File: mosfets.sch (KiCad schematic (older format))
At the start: 72 parts, among them P5 CONN_01X08, P6 CONN_01X06, Q1 2N7002P, Q10 2N7002P, Q11 2N7002P, Q12 BC846BPDW1, Q13 BC846BPDW1, Q14 SI2318CDS-T1-GE3, Q15 IRFB7545PbF, Q16 2N7002P, Q17 2N7002P, Q18 BC846BPDW1, Q19 BC846BPDW1, Q2 2N7002P, Q20 SI2318CDS-T1-GE3, Q21 IRFB7545PbF, Q3 2N7002P, Q4 BC846BPDW1, Q5 BC846BPDW1, Q6 BC846BPDW1, Q7 IRFB7545PbF, Q8 SI2318CDS-T1-GE3, Q9 IRFB7545PbF

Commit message: more schematics
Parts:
- R11, R12, R21, R29: value 1K8 -> 4K7; footprint Resistors_SMD:R_0603 -> Resistors_SMD:R_0805
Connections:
- net +12V: no longer R10.1, R11.1, R12.1, R21.1, R29.1
- net Vheatbed: now also R10.1
- net Vsupply: now also R11.1, R12.1, R21.1, R29.1
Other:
- moved on the sheet: R10, R11, R12, R20, R21, R28, R29

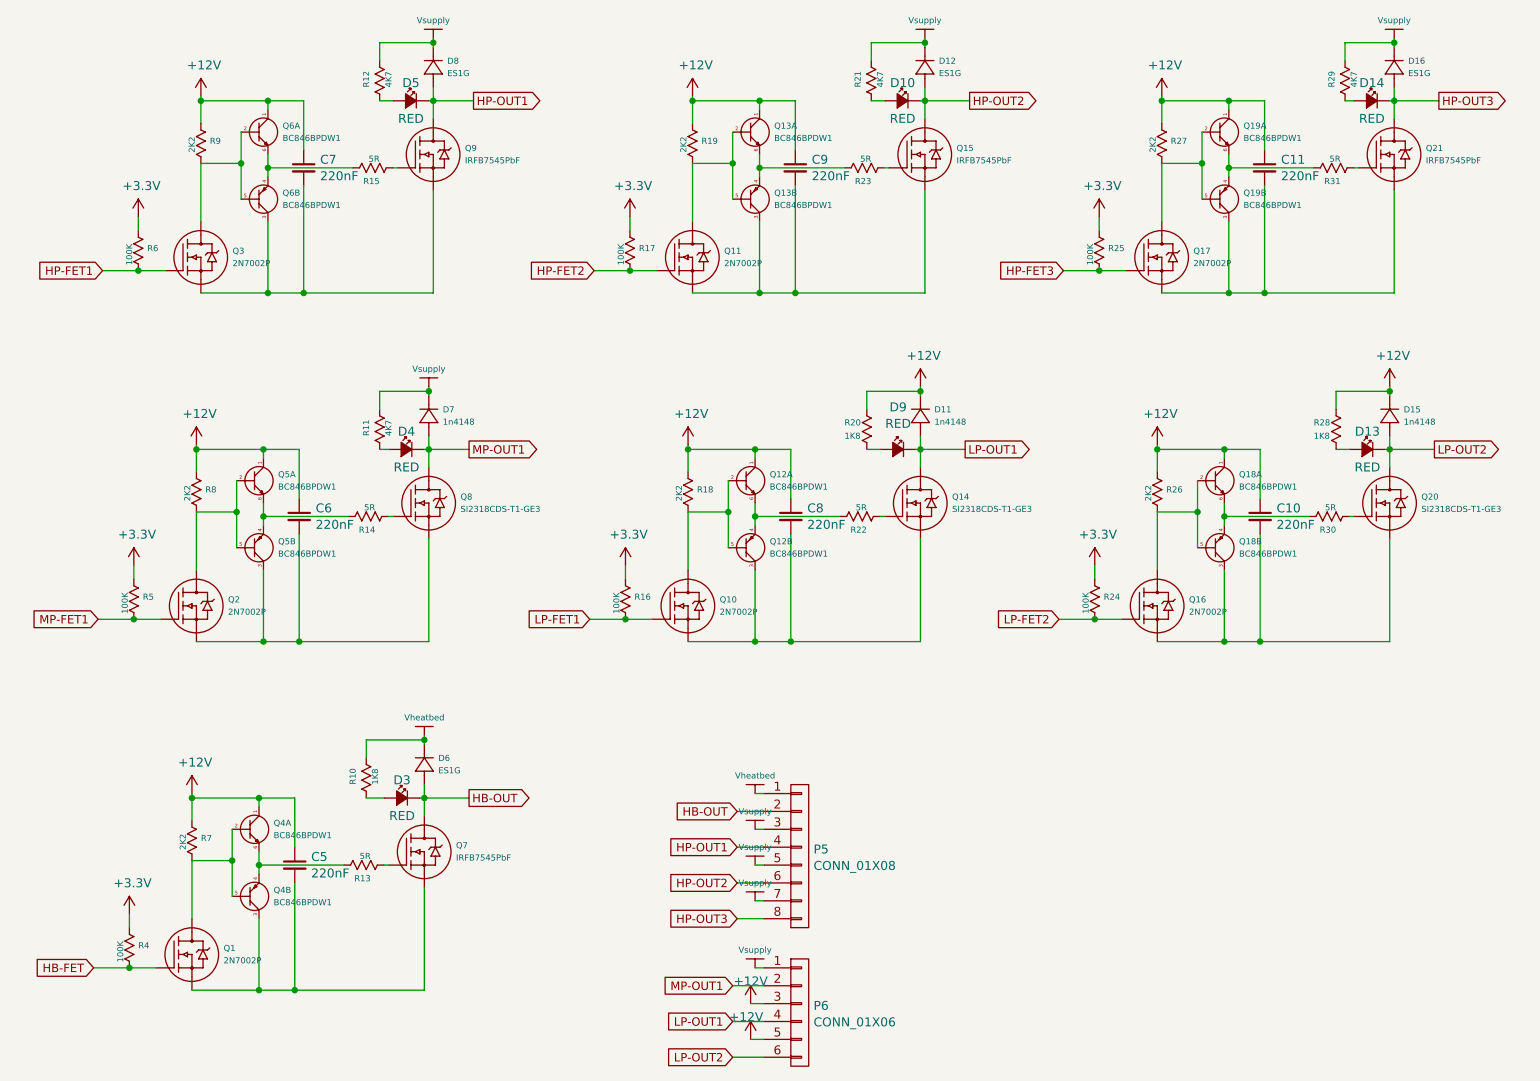
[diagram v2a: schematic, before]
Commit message: more placement and routing
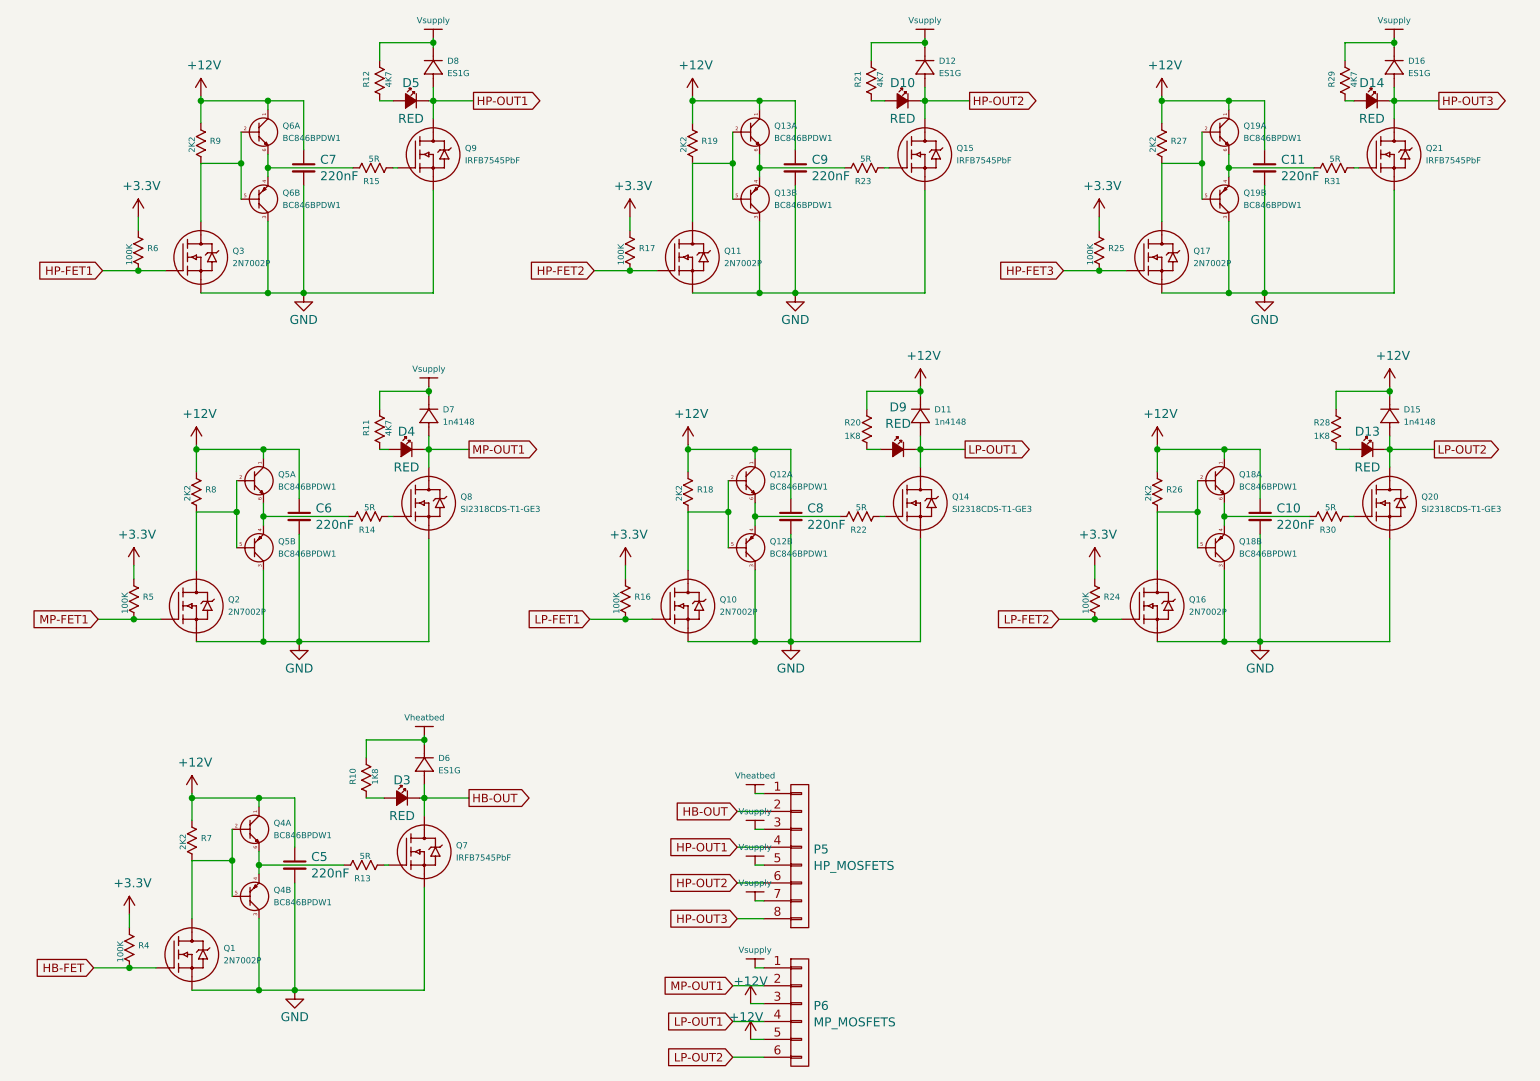
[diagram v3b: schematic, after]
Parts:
- P5: value CONN_01X08 -> HP_MOSFETS
- P6: value CONN_01X06 -> MP_MOSFETS
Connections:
- net GND: now reaches C7.2, Q3.2 (S), Q6.3 (C), Q9.3 (S)
- net GND: now also C10.2, C11.2, C5.2, C6.2, C8.2, C9.2, Q1.2 (S), Q10.2 (S), Q11.2 (S), Q12.3 (C), Q13.3 (C), Q14.3 (S), Q15.3 (S), Q16.2 (S), Q17.2 (S), Q18.3 (C), Q19.3 (C), Q2.2 (S), Q20.3 (S), Q21.3 (S), Q4.3 (C), Q5.3 (C), Q7.3 (S), Q8.3 (S)
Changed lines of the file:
@@
 EESchema Schematic File Version 2
+LIBS:led_reverse
 LIBS:arduino_shieldsNCL
 LIBS:otheruse_transistors
@@
 $EndComp
 $Comp
-L +12V #PWR016
+L +12V #PWR018
 U 1 1 568AF586
 P 1825 1175
-F 0 "#PWR016" H 1825 1025 50  0001 C CNN
+F 0 "#PWR018" H 1825 1025 50  0001 C CNN
 F 1 "+12V" H 1843 1349 50  0000 C CNN
 F 2 "" H 1825 1175 50  0000 C CNN
@@
 $EndComp
 $Comp
-L +3.3V #PWR017
+L +3.3V #PWR019
 U 1 1 568AF93B
 P 1475 1850
-F 0 "#PWR017" H 1475 1700 50  0001 C CNN
+F 0 "#PWR019" H 1475 1700 50  0001 C CNN
 F 1 "+3.3V" H 1493 2024 50  0000 C CNN
 F 2 "" H 1475 1850 50  0000 C CNN
@@
 $EndComp
 $Comp
-L Vsupply #P018
+L Vsupply #P020
 U 1 1 568AFFE8
 P 3125 700
-F 0 "#P018" H 3125 700 60  0001 C CNN
+F 0 "#P020" H 3125 700 60  0001 C CNN
 F 1 "Vsupply" H 3125 650 34  0000 C CNN
 F 2 "" H 3125 700 60  0000 C CNN
@@
 $EndComp
 $Comp
-L +12V #PWR019
+L +12V #PWR021
 U 1 1 568B243B
 P 7200 1175
-F 0 "#PWR019" H 7200 1025 50  0001 C CNN
+F 0 "#PWR021" H 7200 1025 50  0001 C CNN
 F 1 "+12V" H 7218 1349 50  0000 C CNN
 F 2 "" H 7200 1175 50  0000 C CNN
@@
 $EndComp
 $Comp
-L +3.3V #PWR020
+L +3.3V #PWR022
 U 1 1 568B2466
 P 6850 1850
-F 0 "#PWR020" H 6850 1700 50  0001 C CNN
+F 0 "#PWR022" H 6850 1700 50  0001 C CNN
 F 1 "+3.3V" H 6868 2024 50  0000 C CNN
 F 2 "" H 6850 1850 50  0000 C CNN
@@
 $EndComp
 $Comp
-L Vsupply #P021
+L Vsupply #P023
 U 1 1 568B248A
 P 8500 700
-F 0 "#P021" H 8500 700 60  0001 C CNN
+F 0 "#P023" H 8500 700 60  0001 C CNN
 F 1 "Vsupply" H 8500 650 34  0000 C CNN
 F 2 "" H 8500 700 60  0000 C CNN
@@
 $EndComp
 $Comp
-L +12V #PWR022
+L +12V #PWR024
 U 1 1 568B41E7
 P 1775 5075
-F 0 "#PWR022" H 1775 4925 50  0001 C CNN
+F 0 "#PWR024" H 1775 4925 50  0001 C CNN
 F 1 "+12V" H 1793 5249 50  0000 C CNN
 F 2 "" H 1775 5075 50  0000 C CNN
@@
 $EndComp
 $Comp
-L +3.3V #PWR023
+L +3.3V #PWR025
 U 1 1 568B4212
 P 1425 5750
-F 0 "#PWR023" H 1425 5600 50  0001 C CNN
+F 0 "#PWR025" H 1425 5600 50  0001 C CNN
 F 1 "+3.3V" H 1443 5924 50  0000 C CNN
 F 2 "" H 1425 5750 50  0000 C CNN
@@
 $EndComp
 $Comp
-L Vheatbed #P024
+L Vheatbed #P026
 U 1 1 568B479B
 P 3075 4600
-F 0 "#P024" H 3075 4600 60  0001 C CNN
+F 0 "#P026" H 3075 4600 60  0001 C CNN
 F 1 "Vheatbed" H 3075 4550 34  0000 C CNN
 F 2 "" H 3075 4600 60  0000 C CNN
@@
 $EndComp
 $Comp
-L +12V #PWR025
+L +12V #PWR027
 U 1 1 568B79BE
 P 1800 3125
-F 0 "#PWR025" H 1800 2975 50  0001 C CNN
+F 0 "#PWR027" H 1800 2975 50  0001 C CNN
 F 1 "+12V" H 1818 3299 50  0000 C CNN
 F 2 "" H 1800 3125 50  0000 C CNN
@@
 $EndComp
 $Comp
-L +3.3V #PWR026
+L +3.3V #PWR028
 U 1 1 568B79E3
 P 1450 3800
-F 0 "#PWR026" H 1450 3650 50  0001 C CNN
+F 0 "#PWR028" H 1450 3650 50  0001 C CNN
 F 1 "+3.3V" H 1468 3974 50  0000 C CNN
 F 2 "" H 1450 3800 50  0000 C CNN
@@
 $EndComp
 $Comp
-L Vsupply #P027
+L Vsupply #P029
 U 1 1 568B7A06
 P 3100 2650
-F 0 "#P027" H 3100 2650 60  0001 C CNN
+F 0 "#P029" H 3100 2650 60  0001 C CNN
 F 1 "Vsupply" H 3100 2600 34  0000 C CNN
 F 2 "" H 3100 2650 60  0000 C CNN
@@
 $EndComp
 $Comp
-L +12V #PWR028
+L +12V #PWR030
 U 1 1 568B7A31
 P 4550 3125
-F 0 "#PWR028" H 4550 2975 50  0001 C CNN
+F 0 "#PWR030" H 4550 2975 50  0001 C CNN
 F 1 "+12V" H 4568 3299 50  0000 C CNN
 F 2 "" H 4550 3125 50  0000 C CNN
@@
 $EndComp
 $Comp
-L +3.3V #PWR029
+L +3.3V #PWR031
 U 1 1 568B7A56
 P 4200 3800
-F 0 "#PWR029" H 4200 3650 50  0001 C CNN
+F 0 "#PWR031" H 4200 3650 50  0001 C CNN
 F 1 "+3.3V" H 4218 3974 50  0000 C CNN
 F 2 "" H 4200 3800 50  0000 C CNN
@@
 $EndComp
 $Comp
-L +12V #PWR030
+L +12V #PWR032
 U 1 1 568B7AA4
 P 7175 3125
-F 0 "#PWR030" H 7175 2975 50  0001 C CNN
+F 0 "#PWR032" H 7175 2975 50  0001 C CNN
 F 1 "+12V" H 7193 3299 50  0000 C CNN
 F 2 "" H 7175 3125 50  0000 C CNN
@@
 $EndComp
 $Comp
-L +3.3V #PWR031
+L +3.3V #PWR033
 U 1 1 568B7AC9
 P 6825 3800
-F 0 "#PWR031" H 6825 3650 50  0001 C CNN
+F 0 "#PWR033" H 6825 3650 50  0001 C CNN
 F 1 "+3.3V" H 6843 3974 50  0000 C CNN
 F 2 "" H 6825 3800 50  0000 C CNN
@@
 $EndComp
 $Comp
-L +12V #PWR032
+L +12V #PWR034
 U 1 1 568BB35D
 P 5850 2800
-F 0 "#PWR032" H 5850 2650 50  0001 C CNN
+F 0 "#PWR034" H 5850 2650 50  0001 C CNN
 F 1 "+12V" H 5868 2974 50  0000 C CNN
 F 2 "" H 5850 2800 50  0000 C CNN
@@
 $EndComp
 $Comp
-L +12V #PWR033
+L +12V #PWR035
 U 1 1 568BB44F
 P 8475 2800
-F 0 "#PWR033" H 8475 2650 50  0001 C CNN
+F 0 "#PWR035" H 8475 2650 50  0001 C CNN
 F 1 "+12V" H 8493 2974 50  0000 C CNN
 F 2 "" H 8475 2800 50  0000 C CNN
@@
 P 5175 6300
 F 0 "P6" H 5252 6338 50  0000 L CNN
-F 1 "CONN_01X06" H 5252 6246 50  0000 L CNN
+F 1 "MP_MOSFETS" H 5252 6246 50  0000 L CNN
 F 2 "geda-footprints:CON_SCRW_6_PIN_5mm" H 5175 6300 50  0001 C CNN
 F 3 "" H 5175 6300 50  0000 C CNN
@@
 P 5175 5425
 F 0 "P5" H 5252 5463 50  0000 L CNN
-F 1 "CONN_01X08" H 5252 5371 50  0000 L CNN
+F 1 "HP_MOSFETS" H 5252 5371 50  0000 L CNN
 F 2 "geda-footprints:CON_SCRW_8_PIN_5mm" H 5175 5425 50  0001 C CNN
 F 3 "" H 5175 5425 50  0000 C CNN
@@
 $EndComp
 $Comp
-L Vheatbed #P034
+L Vheatbed #P036
 U 1 1 568B0A81
 P 4925 4925
-F 0 "#P034" H 4925 4925 60  0001 C CNN
+F 0 "#P036" H 4925 4925 60  0001 C CNN
 F 1 "Vheatbed" H 4925 4875 34  0000 C CNN
 F 2 "" H 4925 4925 60  0000 C CNN
@@
 $EndComp
 $Comp
-L Vsupply #P035
+L Vsupply #P037
 U 1 1 568B0DA2
 P 4925 5125
-F 0 "#P035" H 4925 5125 60  0001 C CNN
+F 0 "#P037" H 4925 5125 60  0001 C CNN
 F 1 "Vsupply" H 4925 5075 34  0000 C CNN
 F 2 "" H 4925 5125 60  0000 C CNN
@@
 $EndComp
 $Comp
-L Vsupply #P036
+L Vsupply #P038
 U 1 1 568B1161
 P 4925 5325
-F 0 "#P036" H 4925 5325 60  0001 C CNN
+F 0 "#P038" H 4925 5325 60  0001 C CNN
 F 1 "Vsupply" H 4925 5275 34  0000 C CNN
 F 2 "" H 4925 5325 60  0000 C CNN
@@
 HP-OUT1
 $Comp
-L Vsupply #P037
+L Vsupply #P039
 U 1 1 568BBE8C
 P 4925 5525
-F 0 "#P037" H 4925 5525 60  0001 C CNN
+F 0 "#P039" H 4925 5525 60  0001 C CNN
 F 1 "Vsupply" H 4925 5475 34  0000 C CNN
 F 2 "" H 4925 5525 60  0000 C CNN
@@
 HP-OUT3
 $Comp
-L Vsupply #P038
+L Vsupply #P040
 U 1 1 568BDAE4
 P 4925 5900
-F 0 "#P038" H 4925 5900 60  0001 C CNN
+F 0 "#P040" H 4925 5900 60  0001 C CNN
 F 1 "Vsupply" H 4925 5850 34  0000 C CNN
 F 2 "" H 4925 5900 60  0000 C CNN
@@
 $EndComp
 $Comp
-L +12V #PWR039
+L +12V #PWR041
 U 1 1 568BDD67
 P 4900 6250
-F 0 "#PWR039" H 4900 6100 50  0001 C CNN
+F 0 "#PWR041" H 4900 6100 50  0001 C CNN
 F 1 "+12V" H 4900 6375 50  0000 C CNN
 F 2 "" H 4900 6250 50  0000 C CNN
@@
 $EndComp
 $Comp
-L +12V #PWR040
+L +12V #PWR042
 U 1 1 568BE300
 P 4900 6450
-F 0 "#PWR040" H 4900 6300 50  0001 C CNN
+F 0 "#PWR042" H 4900 6300 50  0001 C CNN
 F 1 "+12V" H 4875 6575 50  0000 C CNN
 F 2 "" H 4900 6450 50  0000 C CNN
@@
 $EndComp
 $Comp
-L Vsupply #P041
+L Vsupply #P043
 U 1 1 568B1D38
 P 5875 700
-F 0 "#P041" H 5875 700 60  0001 C CNN
+F 0 "#P043" H 5875 700 60  0001 C CNN
 F 1 "Vsupply" H 5875 650 34  0000 C CNN
 F 2 "" H 5875 700 60  0000 C CNN
@@
 $EndComp
 $Comp
-L +3.3V #PWR042
+L +3.3V #PWR044
 U 1 1 568B1D14
 P 4225 1850
-F 0 "#PWR042" H 4225 1700 50  0001 C CNN
+F 0 "#PWR044" H 4225 1700 50  0001 C CNN
 F 1 "+3.3V" H 4243 2024 50  0000 C CNN
 F 2 "" H 4225 1850 50  0000 C CNN
@@
 $EndComp
 $Comp
-L +12V #PWR043
+L +12V #PWR045
 U 1 1 568B1CE9
 P 4575 1175
-F 0 "#PWR043" H 4575 1025 50  0001 C CNN
+F 0 "#PWR045" H 4575 1025 50  0001 C CNN
 F 1 "+12V" H 4593 1349 50  0000 C CNN
 F 2 "" H 4575 1175 50  0000 C CNN
@@
 	-1   0    0    -1
 $EndComp
+$Comp
+L GND #PWR046
+U 1 1 568FBDE7
+P 2400 2275
+F 0 "#PWR046" H 2400 2025 50  0001 C CNN
+F 1 "GND" H 2400 2125 50  0000 C CNN
+F 2 "" H 2400 2275 50  0000 C CNN
+F 3 "" H 2400 2275 50  0000 C CNN
+	1    2400 2275
+	1    0    0    -1
+$EndComp
+$Comp
+L GND #PWR047
+U 1 1 568FC7E3
+P 2375 4225
+F 0 "#PWR047" H 2375 3975 50  0001 C CNN
+F 1 "GND" H 2375 4075 50  0000 C CNN
+F 2 "" H 2375 4225 50  0000 C CNN
+F 3 "" H 2375 4225 50  0000 C CNN
+	1    2375 4225
+	1    0    0    -1
+$EndComp
+$Comp
+L GND #PWR048
+U 1 1 568FCBA2
+P 2350 6175
+F 0 "#PWR048" H 2350 5925 50  0001 C CNN
+F 1 "GND" H 2350 6025 50  0000 C CNN
+F 2 "" H 2350 6175 50  0000 C CNN
+F 3 "" H 2350 6175 50  0000 C CNN
+	1    2350 6175
+	1    0    0    -1
+$EndComp
+$Comp
+L GND #PWR049
+U 1 1 568FCF61
+P 5125 4225
+F 0 "#PWR049" H 5125 3975 50  0001 C CNN
+F 1 "GND" H 5125 4075 50  0000 C CNN
+F 2 "" H 5125 4225 50  0000 C CNN
+F 3 "" H 5125 4225 50  0000 C CNN
+	1    5125 4225
+	1    0    0    -1
+$EndComp
+$Comp
+L GND #PWR050
+U 1 1 568FD2D1
+P 7750 4225
+F 0 "#PWR050" H 7750 3975 50  0001 C CNN
+F 1 "GND" H 7750 4075 50  0000 C CNN
+F 2 "" H 7750 4225 50  0000 C CNN
+F 3 "" H 7750 4225 50  0000 C CNN
+	1    7750 4225
+	1    0    0    -1
+$EndComp
+$Comp
+L GND #PWR051
+U 1 1 568FD5A3
+P 7775 2275
+F 0 "#PWR051" H 7775 2025 50  0001 C CNN
+F 1 "GND" H 7775 2125 50  0000 C CNN
+F 2 "" H 7775 2275 50  0000 C CNN
+F 3 "" H 7775 2275 50  0000 C CNN
+	1    7775 2275
+	1    0    0    -1
+$EndComp
+$Comp
+L GND #PWR052
+U 1 1 568FDA4F
+P 5150 2275
+F 0 "#PWR052" H 5150 2025 50  0001 C CNN
+F 1 "GND" H 5150 2125 50  0000 C CNN
+F 2 "" H 5150 2275 50  0000 C CNN
+F 3 "" H 5150 2275 50  0000 C CNN
+	1    5150 2275
+	1    0    0    -1
+$EndComp
 $EndSCHEMATC

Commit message: More routing
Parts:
- D10, D13, D14, D3, D4, D5, D9: footprint geda-footprints:0603diode -> armin-footprints:0603diode
- D11, D15, D7: footprint geda-footprints:LL-34 -> armin-footprints:LL-34
- D12, D16, D6, D8: footprint geda-footprints:DO214AC -> armin-footprints:DO214AC
- Q1, Q10, Q11, Q14, Q16, Q17, Q2, Q20, Q3, Q8: footprint geda-footprints:SOT23_3L -> armin-footprints:SOT23_3L
- Q12, Q13, Q18, Q19, Q4, Q5, Q6: footprint geda-footprints:SC70_6L -> armin-footprints:SC70_6L
- Q15, Q21, Q7, Q9: footprint geda-footprints:TO-220 -> armin-footprints:TO-220
- R10: value 1K8 -> 4K7; footprint Resistors_SMD:R_0603 -> Resistors_SMD:R_0805

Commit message: Added 3d models
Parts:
- P5: footprint geda-footprints:CON_SCRW_8_PIN_5mm -> armin-footprints:TERMINAL_BLOCK_8_PIN_5mm
- P6: footprint geda-footprints:CON_SCRW_6_PIN_5mm -> armin-footprints:TERMINAL_BLOCK_6_PIN_5mm
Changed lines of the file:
@@
 F 0 "P6" H 5252 6338 50  0000 L CNN
 F 1 "MP_MOSFETS" H 5252 6246 50  0000 L CNN
-F 2 "geda-footprints:CON_SCRW_6_PIN_5mm" H 5175 6300 50  0001 C CNN
+F 2 "armin-footprints:TERMINAL_BLOCK_6_PIN_5mm" H 5175 6300 50  0001 C CNN
 F 3 "" H 5175 6300 50  0000 C CNN
 	1    5175 6300
@@
 F 0 "P5" H 5252 5463 50  0000 L CNN
 F 1 "HP_MOSFETS" H 5252 5371 50  0000 L CNN
-F 2 "geda-footprints:CON_SCRW_8_PIN_5mm" H 5175 5425 50  0001 C CNN
+F 2 "armin-footprints:TERMINAL_BLOCK_8_PIN_5mm" H 5175 5425 50  0001 C CNN
 F 3 "" H 5175 5425 50  0000 C CNN
 	1    5175 5425

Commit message: More 3d stuff
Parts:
- C10, C11, C5, C6, C7, C8, C9: footprint Capacitors_SMD:C_0603 -> capacitors:C_0603
- D10, D13, D14, D3, D4, D5, D9: footprint armin-footprints:0603diode -> diodes:LED-0603
- D11, D15, D7: footprint armin-footprints:LL-34 -> diodes:SOD-80C
- D12, D16, D6, D8: footprint armin-footprints:DO214AC -> diodes:DO214AC_SMA
- P5: footprint armin-footprints:TERMINAL_BLOCK_8_PIN_5mm -> terminal_blocks:TERMINAL_BLOCK_8_PIN_5mm
- P6: footprint armin-footprints:TERMINAL_BLOCK_6_PIN_5mm -> terminal_blocks:TERMINAL_BLOCK_6_PIN_5mm
- Q1, Q10, Q11, Q14, Q16, Q17, Q2, Q20, Q3, Q8: footprint armin-footprints:SOT23_3L -> sot:SOT23_3L
- Q12, Q13, Q18, Q19, Q4, Q5, Q6: footprint armin-footprints:SC70_6L -> sot:SC70_6L
- Q15, Q21, Q9: footprint armin-footprints:TO-220 -> to:TO-220
- Q7: footprint armin-footprints:TO-220 -> (none)
- R13, R14, R15, R16, R17, R18, R19, R20, R22, R23, R24, R25, R26, R27, R28, R30, R31, R4, R5, R6, R7, R8, R9: footprint Resistors_SMD:R_0603 -> resistors:R_0603

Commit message: cleanup
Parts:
- Q7: footprint (none) -> to:TO-220
- R10, R11, R12, R21, R29: footprint Resistors_SMD:R_0805 -> resistors:R_0805
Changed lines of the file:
@@
 F 0 "R12" H 2950 925 34  0000 R CNN
 F 1 "4K7" H 2950 1050 34  0000 R CNN
-F 2 "Resistors_SMD:R_0805" H 2800 975 60  0001 C CNN
+F 2 "resistors:R_0805" H 2800 975 60  0001 C CNN
 F 3 "" H 2800 975 60  0000 C CNN
 	1    2800 975
@@
 F 0 "R29" H 8350 925 34  0000 R CNN
 F 1 "4K7" H 8350 1050 34  0000 R CNN
-F 2 "Resistors_SMD:R_0805" H 8200 975 60  0001 C CNN
+F 2 "resistors:R_0805" H 8200 975 60  0001 C CNN
 F 3 "" H 8200 975 60  0000 C CNN
 	1    8200 975
@@
 F 0 "R10" H 2875 4825 34  0000 R CNN
 F 1 "4K7" H 2875 4950 34  0000 R CNN
-F 2 "Resistors_SMD:R_0805" H 2725 4875 60  0001 C CNN
+F 2 "resistors:R_0805" H 2725 4875 60  0001 C CNN
 F 3 "" H 2725 4875 60  0000 C CNN
 	1    2725 4875
@@
 F 0 "Q7" H 3252 5835 34  0000 L CNN
 F 1 "IRFB7545PbF" H 3252 5766 34  0000 L CNN
-F 2 "" H 2875 5600 60  0001 C CNN
+F 2 "to:TO-220" H 2875 5600 60  0001 C CNN
 F 3 "" H 2875 5600 60  0000 C CNN
 	1    2875 5600
@@
 F 0 "R11" H 2950 2875 34  0000 R CNN
 F 1 "4K7" H 2950 3000 34  0000 R CNN
-F 2 "Resistors_SMD:R_0805" H 2800 2925 60  0001 C CNN
+F 2 "resistors:R_0805" H 2800 2925 60  0001 C CNN
 F 3 "" H 2800 2925 60  0000 C CNN
 	1    2800 2925
@@
 F 0 "R21" H 5700 925 34  0000 R CNN
 F 1 "4K7" H 5700 1050 34  0000 R CNN
-F 2 "Resistors_SMD:R_0805" H 5550 975 60  0001 C CNN
+F 2 "resistors:R_0805" H 5550 975 60  0001 C CNN
 F 3 "" H 5550 975 60  0000 C CNN
 	1    5550 975
